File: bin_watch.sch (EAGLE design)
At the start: 88 parts, among them IC1 MEGA48/88/168-AU, J1 USB3100-XX-X_REVB, Q1 32.768kHz, T1 2N7002BKV, T2 2N7002BKV, T3 2N7002BKV, T4 2N7002BKV, T5 PMDT670UPE, T6 PMDT670UPE, T7 PMDT670UPE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

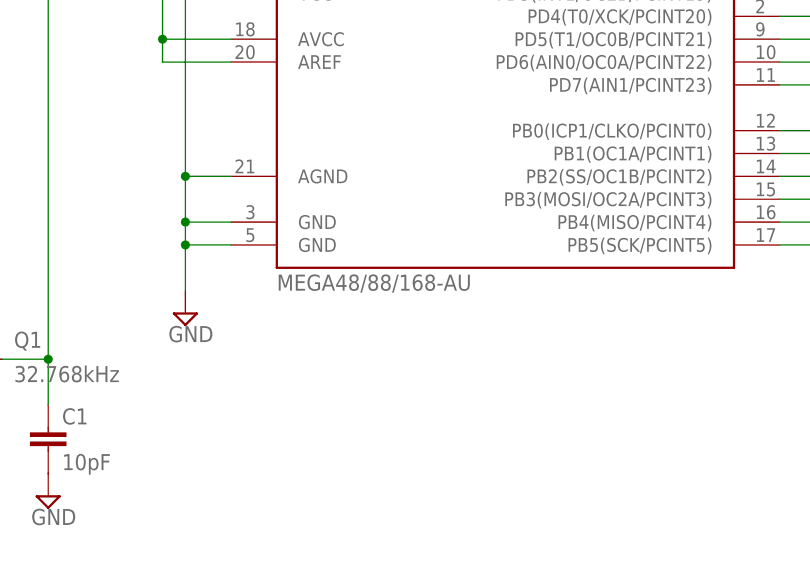
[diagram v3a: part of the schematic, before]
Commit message: QFN
ATmega328 now a QFN-32
TODO: place components, route
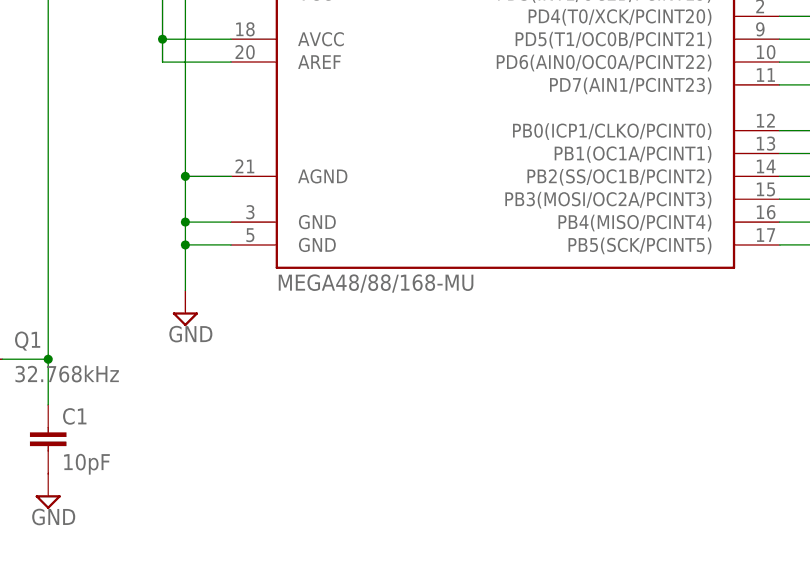
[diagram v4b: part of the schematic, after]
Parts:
- IC1: value MEGA48/88/168-AU -> MEGA48/88/168-MU; device avr-5:MEGA48/88/168-AU -> avr-5:MEGA48/88/168-MU
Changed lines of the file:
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@@
 </variantdefs>
 <classes>
-<class number="0" name="default" width="0.16" drill="0">
+<class number="0" name="default" width="0.16" drill="0.3">
 <clearance class="0" value="0.16"/>
 </class>
-<class number="1" name="supply" width="0.2" drill="0">
+<class number="1" name="supply" width="0.2" drill="0.35">
 <clearance class="1" value="0.2"/>
 </class>
-<class number="2" name="clock" width="0.16" drill="0">
+<class number="2" name="clock" width="0.16" drill="0.3">
 <clearance class="2" value="0.2"/>
 </class>
-<class number="3" name="pwr" width="0.2" drill="0">
+<class number="3" name="pwr" width="0.2" drill="0.35">
 <clearance class="3" value="0.2"/>
+</class>
+<class number="4" name="signal" width="0.127" drill="0.254">
+<clearance class="4" value="0.127"/>
 </class>
 </classes>
@@
 <part name="SUPPLY2" library="supply2" library_urn="urn:adsk.eagle:library:372" deviceset="GND" device=""/>
 <part name="JP1" library="avr-5" deviceset="AVR-ISP-6" device=""/>
-<part name="IC1" library="avr-5" deviceset="MEGA48/88/168" device="-AU"/>
+<part name="IC1" library="avr-5" deviceset="MEGA48/88/168" device="-MU" value="MEGA48/88/168-MU"/>
 <part name="SUPPLY3" library="supply2" library_urn="urn:adsk.eagle:library:372" deviceset="GND" device=""/>
 <part name="D5" library="standardparts" deviceset="LED" device=".0603" value="RG"/>
@@
 </segment>
 </net>
-<net name="GND" class="1">
+<net name="GND" class="4">
 <segment>
 <pinref part="C1" gate="G$1" pin="2"/>
@@
 </segment>
 </net>
-<net name="RST" class="0">
+<net name="RST" class="4">
 <segment>
 <pinref part="JP1" gate="G$1" pin="5"/>
@@
 </segment>
 </net>
-<net name="SCK" class="0">
+<net name="SCK" class="4">
 <segment>
 <pinref part="JP1" gate="G$1" pin="3"/>
@@
 </segment>
 </net>
-<net name="MOSI" class="0">
+<net name="MOSI" class="4">
 <segment>
 <pinref part="JP1" gate="G$1" pin="4"/>
@@
 </segment>
 </net>
-<net name="MISO" class="0">
+<net name="MISO" class="4">
 <segment>
 <pinref part="JP1" gate="G$1" pin="1"/>
@@
 </segment>
 </net>
-<net name="PB0" class="0">
+<net name="PB0" class="4">
 <segment>
 <pinref part="IC1" gate="1" pin="PB0(ICP1/CLKO/PCINT0)"/>
@@
 </segment>
 </net>
-<net name="PB1" class="0">
+<net name="PB1" class="4">
 <segment>
 <pinref part="IC1" gate="1" pin="PB1(OC1A/PCINT1)"/>
@@
 </segment>
 </net>
-<net name="PB2" class="0">
+<net name="PB2" class="4">
 <segment>
 <pinref part="IC1" gate="1" pin="PB2(SS/OC1B/PCINT2)"/>
@@
 </segment>
 </net>
-<net name="PC0" class="0">
+<net name="PC0" class="4">
 <segment>
 <pinref part="IC1" gate="1" pin="PC0(ADC0/PCINT8)"/>
@@
 </segment>
 </net>
-<net name="PC1" class="0">
+<net name="PC1" class="4">
 <segment>
 <pinref part="IC1" gate="1" pin="PC1(ADC1/PCINT9)"/>
@@
 </segment>
 </net>
-<net name="PC2" class="0">
+<net name="PC2" class="4">
 <segment>
 <pinref part="IC1" gate="1" pin="PC2(ADC2/PCINT10)"/>
@@
 </segment>
 </net>
-<net name="PC3" class="0">
+<net name="PC3" class="4">
 <segment>
 <pinref part="IC1" gate="1" pin="PC3(ADC3/PCINT11)"/>
@@
 </segment>
 </net>
-<net name="PC4" class="0">
+<net name="PC4" class="4">
 <segment>
 <pinref part="IC1" gate="1" pin="PC4(ADC4/SDA/PCINT12)"/>
@@
 </segment>
 </net>
-<net name="PC5" class="0">
+<net name="PC5" class="4">
 <segment>
 <pinref part="IC1" gate="1" pin="PC5(ADC5/SCL/PCINT13)"/>
@@
 </segment>
 </net>
-<net name="PD0" class="0">
+<net name="PD0" class="4">
 <segment>
 <pinref part="IC1" gate="1" pin="PD0(RXD/PCINT16)"/>
@@
 </segment>
 </net>
-<net name="PD1" class="0">
+<net name="PD1" class="4">
 <segment>
 <pinref part="IC1" gate="1" pin="PD1(TXD/PCINT17)"/>
@@
 </segment>
 </net>
-<net name="PD2" class="0">
+<net name="PD2" class="4">
 <segment>
 <pinref part="IC1" gate="1" pin="PD2(INT0/PCINT18)"/>
@@
 </segment>
 </net>
-<net name="PD3" class="0">
+<net name="PD3" class="4">
 <segment>
 <pinref part="IC1" gate="1" pin="PD3(INT1/OC2B/PCINT19)"/>
@@
 </segment>
 </net>
-<net name="PD4" class="0">
+<net name="PD4" class="4">
 <segment>
 <pinref part="IC1" gate="1" pin="PD4(T0/XCK/PCINT20)"/>
@@
 </segment>
 </net>
-<net name="PD5" class="0">
+<net name="PD5" class="4">
 <segment>
 <pinref part="IC1" gate="1" pin="PD5(T1/OC0B/PCINT21)"/>
@@
 </segment>
 </net>
-<net name="PD6" class="0">
+<net name="PD6" class="4">
 <segment>
 <pinref part="IC1" gate="1" pin="PD6(AIN0/OC0A/PCINT22)"/>
@@
 </segment>
 </net>
-<net name="PD7" class="0">
+<net name="PD7" class="4">
 <segment>
 <pinref part="IC1" gate="1" pin="PD7(AIN1/PCINT23)"/>
@@
 </segment>
 </net>
-<net name="PROG" class="0">
+<net name="PROG" class="4">
 <segment>
 <pinref part="U1" gate="A" pin="PROG"/>

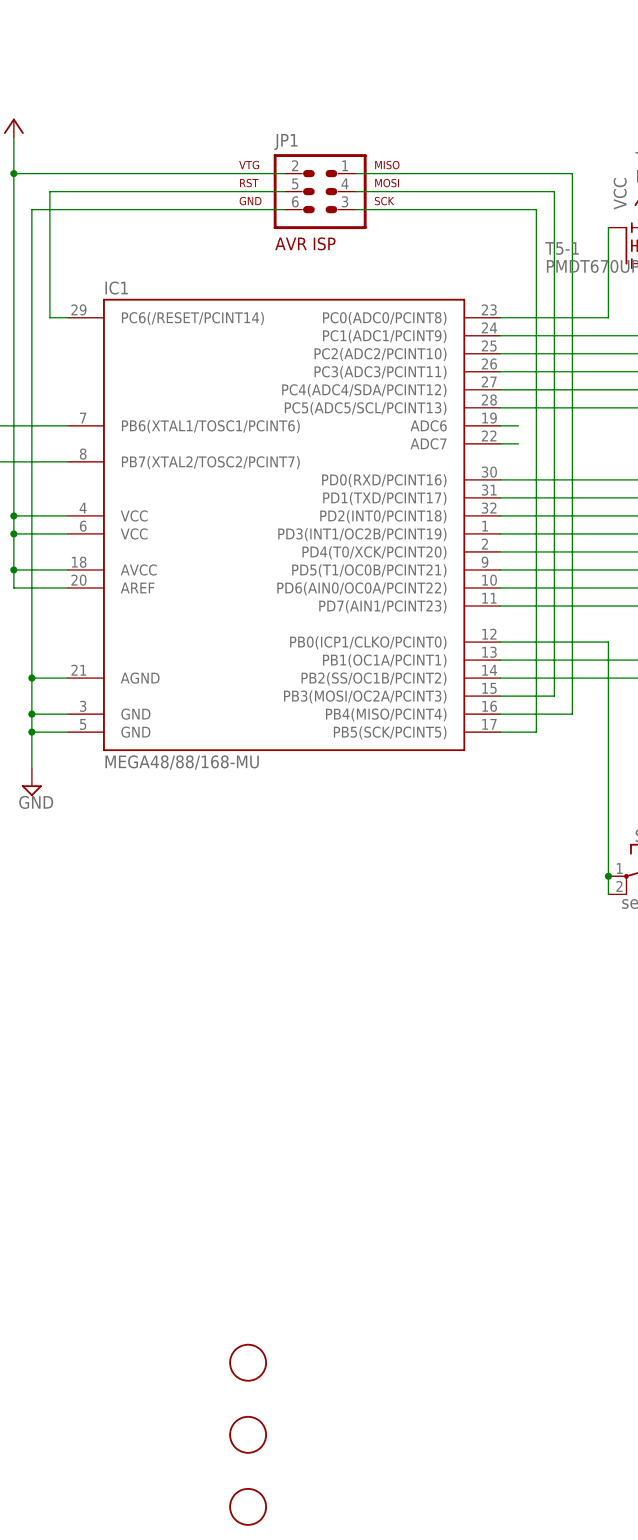
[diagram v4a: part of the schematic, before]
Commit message: Replaced AVR ISP with smaller pads
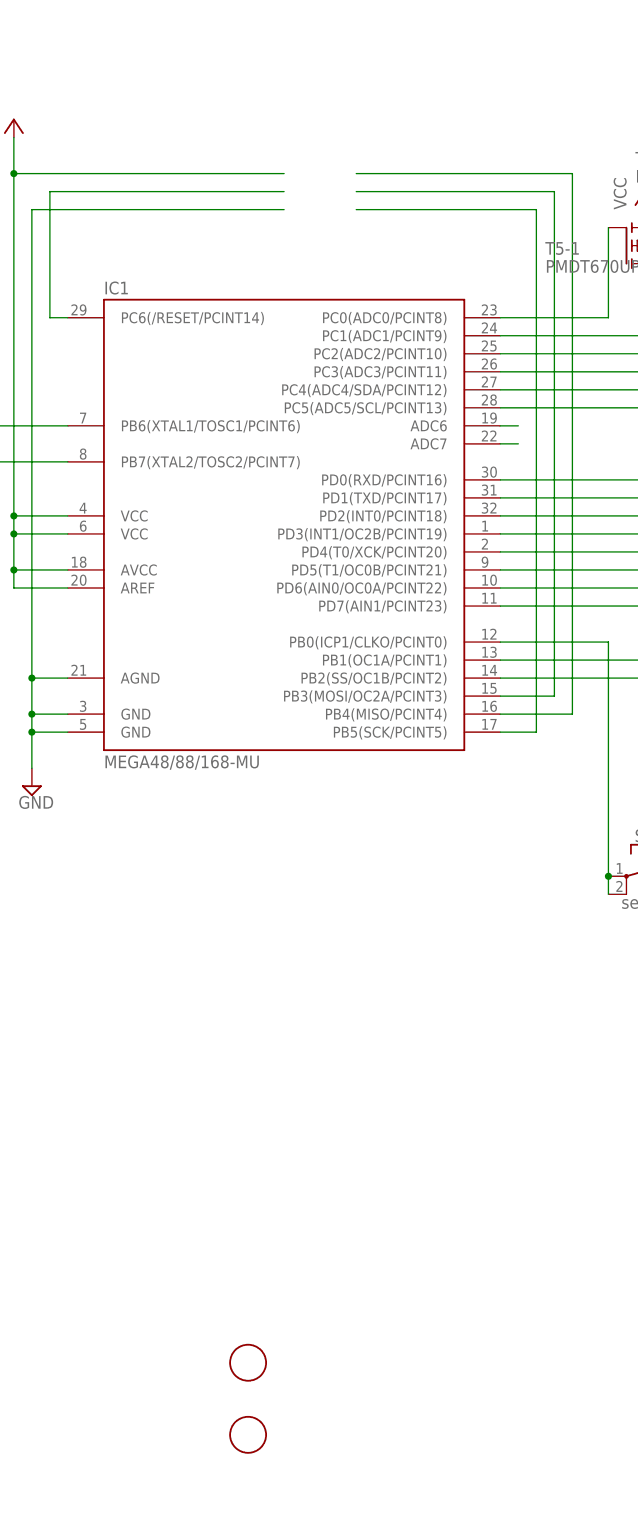
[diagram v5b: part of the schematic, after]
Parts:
- removed JP1: AVR-ISP-6, avr-5:AVR-ISP-6
- removed U$3: FIDUCIAL, adafruit:FIDUCIAL
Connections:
- net GND: no longer JP1.6
- net MISO: no longer JP1.1
- net MOSI: no longer JP1.4
- net RST: no longer JP1.5
- net SCK: no longer JP1.3
- net VCC: no longer JP1.2
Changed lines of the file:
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@@
 <clearance class="3" value="0.2"/>
 </class>
-<class number="4" name="signal" width="0.127" drill="0.254">
-<clearance class="4" value="0.127"/>
+<class number="4" name="signal" width="0.13" drill="0.254">
+<clearance class="4" value="0.13"/>
 </class>
 </classes>
@@
 <part name="C1" library="rcl" library_urn="urn:adsk.eagle:library:334" deviceset="C-EU" device="C0603" package3d_urn="urn:adsk.eagle:package:23616/2" value="10pF"/>
 <part name="SUPPLY2" library="supply2" library_urn="urn:adsk.eagle:library:372" deviceset="GND" device=""/>
-<part name="JP1" library="avr-5" deviceset="AVR-ISP-6" device=""/>
 <part name="IC1" library="avr-5" deviceset="MEGA48/88/168" device="-MU" value="MEGA48/88/168-MU"/>
 <part name="SUPPLY3" library="supply2" library_urn="urn:adsk.eagle:library:372" deviceset="GND" device=""/>
@@
 <part name="U$1" library="adafruit" library_urn="urn:adsk.eagle:library:420" deviceset="FIDUCIAL" device=""/>
 <part name="U$2" library="adafruit" library_urn="urn:adsk.eagle:library:420" deviceset="FIDUCIAL" device=""/>
-<part name="U$3" library="adafruit" library_urn="urn:adsk.eagle:library:420" deviceset="FIDUCIAL" device=""/>
 <part name="U2" library="Texas Instruments_By_element14_Batch_1" deviceset="TPS61240DRVT" device=""/>
 <part name="P+8" library="supply1" library_urn="urn:adsk.eagle:library:371" deviceset="VCC" device=""/>
@@
 <instance part="C1" gate="G$1" x="43.18" y="15.24"/>
 <instance part="SUPPLY2" gate="GND" x="43.18" y="7.62"/>
-<instance part="JP1" gate="G$1" x="99.06" y="111.76"/>
 <instance part="IC1" gate="1" x="93.98" y="66.04"/>
 <instance part="SUPPLY3" gate="GND" x="58.42" y="27.94"/>
@@
 <instance part="U$1" gate="G$1" x="88.9" y="-53.34"/>
 <instance part="U$2" gate="G$1" x="88.9" y="-63.5"/>
-<instance part="U$3" gate="G$1" x="88.9" y="-73.66"/>
 <instance part="U2" gate="A" x="254" y="248.92"/>
 <instance part="P+8" gate="VCC" x="281.94" y="284.48"/>
@@
 </segment>
 </net>
-<net name="GND" class="4">
+<net name="GND" class="1">
 <segment>
 <pinref part="C1" gate="G$1" pin="2"/>
@@
 </segment>
 <segment>
-<pinref part="JP1" gate="G$1" pin="6"/>
 <wire x1="93.98" y1="109.22" x2="58.42" y2="109.22" width="0.1524" layer="91"/>
 <wire x1="58.42" y1="109.22" x2="58.42" y2="43.18" width="0.1524" layer="91"/>
@@
 <net name="RST" class="4">
 <segment>
-<pinref part="JP1" gate="G$1" pin="5"/>
 <wire x1="93.98" y1="111.76" x2="60.96" y2="111.76" width="0.1524" layer="91"/>
 <wire x1="60.96" y1="111.76" x2="60.96" y2="93.98" width="0.1524" layer="91"/>
@@
 <net name="SCK" class="4">
 <segment>
-<pinref part="JP1" gate="G$1" pin="3"/>
 <wire x1="104.14" y1="109.22" x2="129.54" y2="109.22" width="0.1524" layer="91"/>
 <wire x1="129.54" y1="109.22" x2="129.54" y2="35.56" width="0.1524" layer="91"/>
@@
 <net name="MOSI" class="4">
 <segment>
-<pinref part="JP1" gate="G$1" pin="4"/>
 <wire x1="104.14" y1="111.76" x2="132.08" y2="111.76" width="0.1524" layer="91"/>
 <wire x1="132.08" y1="111.76" x2="132.08" y2="40.64" width="0.1524" layer="91"/>
@@
 <net name="MISO" class="4">
 <segment>
-<pinref part="JP1" gate="G$1" pin="1"/>
 <wire x1="104.14" y1="114.3" x2="134.62" y2="114.3" width="0.1524" layer="91"/>
 <wire x1="134.62" y1="114.3" x2="134.62" y2="38.1" width="0.1524" layer="91"/>
@@
 <net name="VCC" class="1">
 <segment>
-<pinref part="JP1" gate="G$1" pin="2"/>
 <wire x1="93.98" y1="114.3" x2="55.88" y2="114.3" width="0.1524" layer="91"/>
 <wire x1="55.88" y1="114.3" x2="55.88" y2="66.04" width="0.1524" layer="91"/>

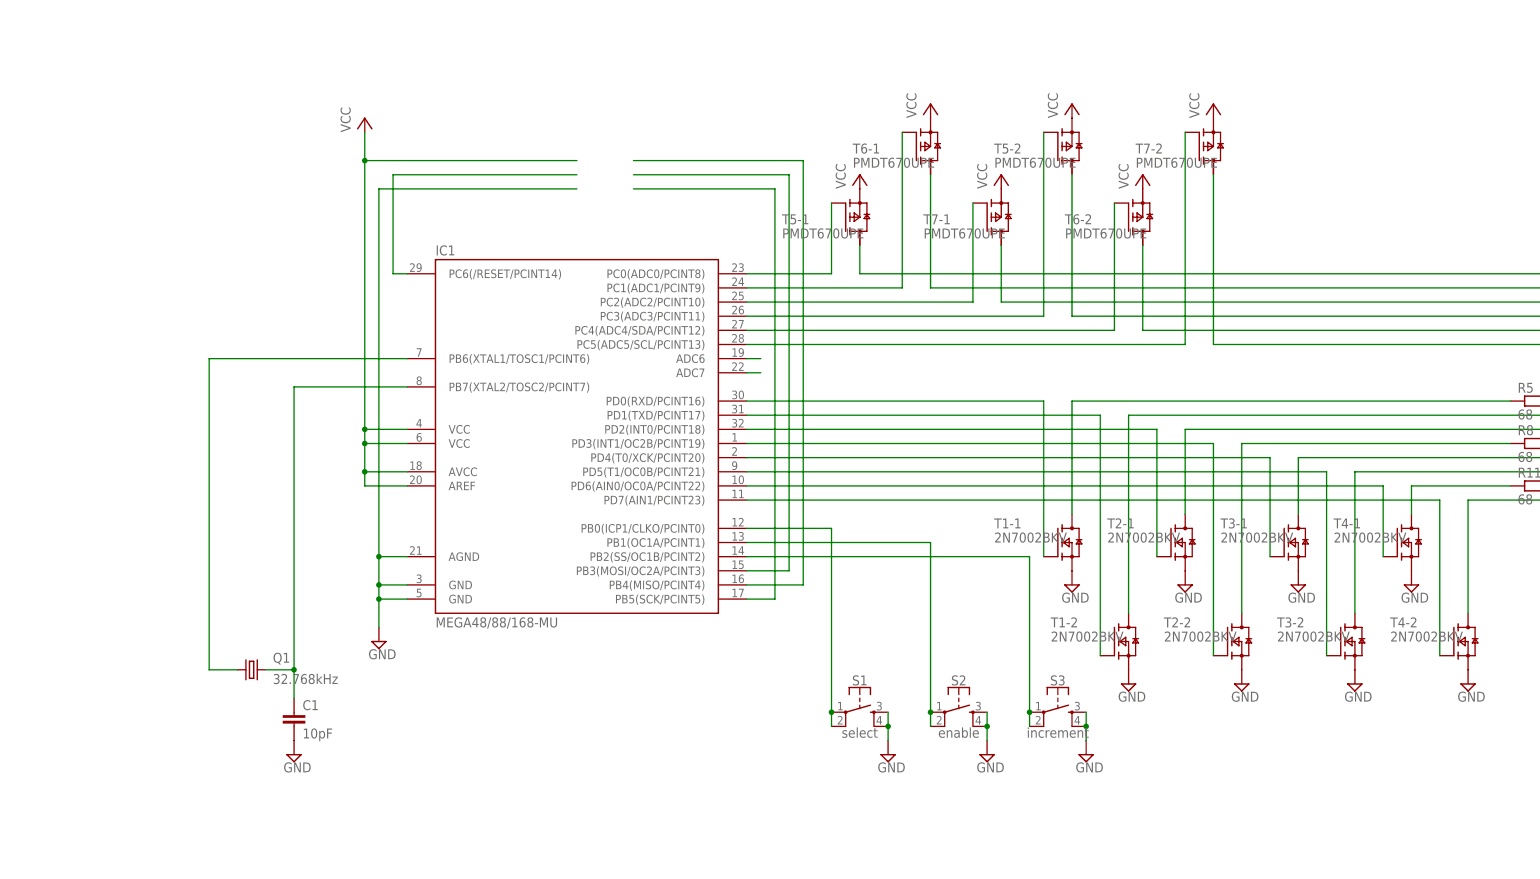
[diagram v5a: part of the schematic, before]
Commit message: IOs rewired
Changed the IO wiring to reduce the number of vias.
TODO: Power supply routing
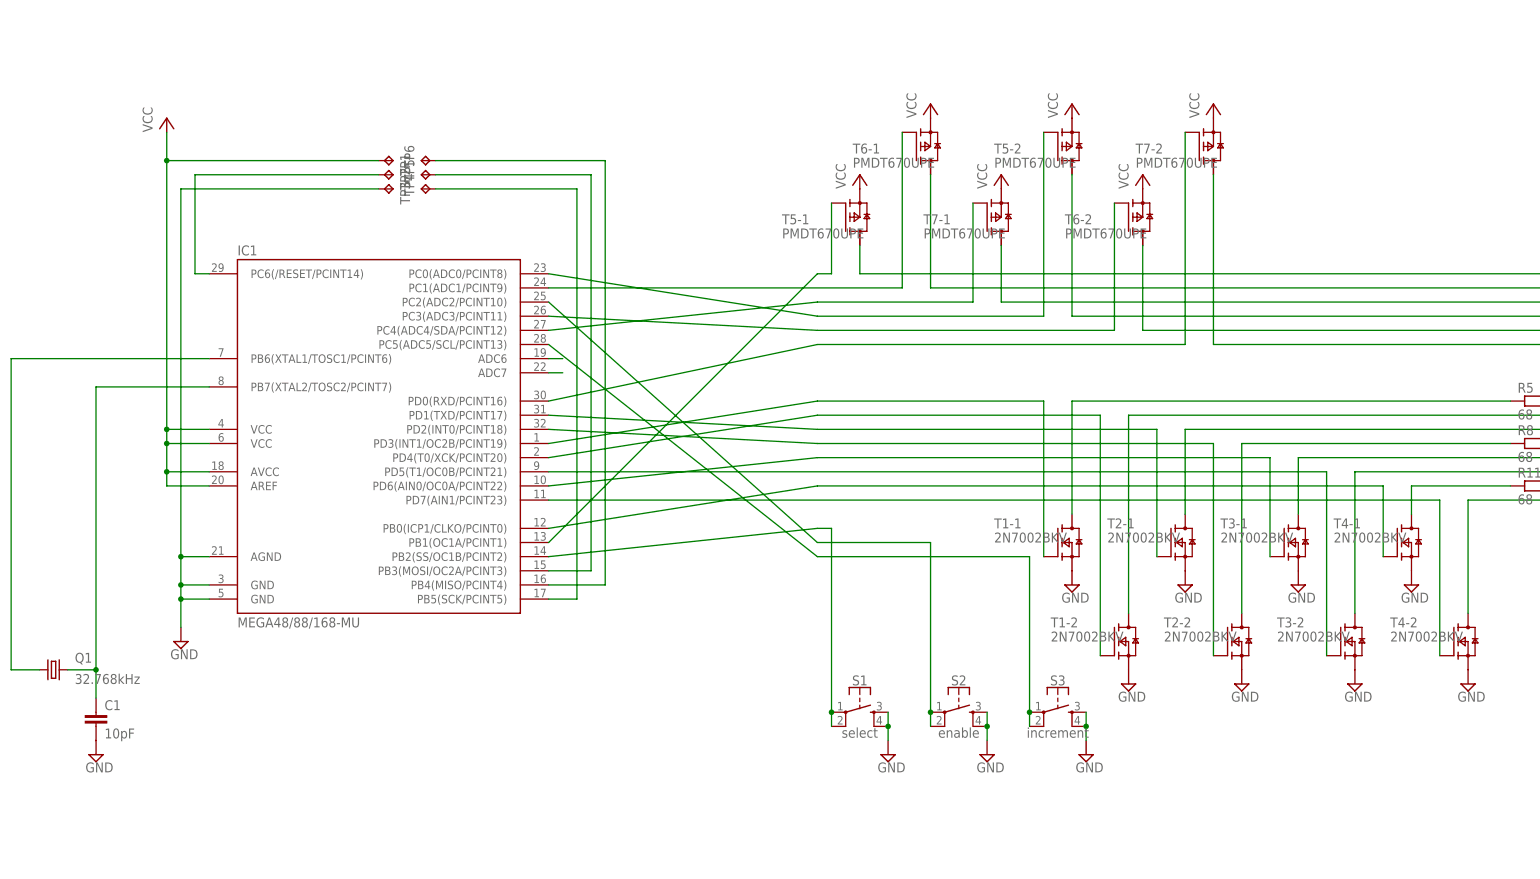
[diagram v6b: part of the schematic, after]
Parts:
- added TP1, TP2, TP3, TP4, TP5, TP6: TPTP07SQ, testpad:TPTP07SQ
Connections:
- net GND: now also TP3.TP
- net MISO: now also TP6.TP
- net MOSI: now also TP5.TP
- net PB0: now also IC1.PB2(SS/OC1B/PCINT2); no longer IC1.PB0(ICP1/CLKO/PCINT0)
- net PB1: now also IC1.PC2(ADC2/PCINT10); no longer IC1.PB1(OC1A/PCINT1)
- net PB2: now also IC1.PC5(ADC5/SCL/PCINT13); no longer IC1.PB2(SS/OC1B/PCINT2)
- net PC0: now also IC1.PB1(OC1A/PCINT1); no longer IC1.PC0(ADC0/PCINT8)
- net PC2: now also IC1.PC4(ADC4/SDA/PCINT12); no longer IC1.PC2(ADC2/PCINT10)
- net PC3: now also IC1.PC0(ADC0/PCINT8); no longer IC1.PC3(ADC3/PCINT11)
- net PC4: now also IC1.PC3(ADC3/PCINT11); no longer IC1.PC4(ADC4/SDA/PCINT12)
- net PC5: now also IC1.PD0(RXD/PCINT16); no longer IC1.PC5(ADC5/SCL/PCINT13)
- net PD0: now also IC1.PD3(INT1/OC2B/PCINT19); no longer IC1.PD0(RXD/PCINT16)
- net PD1: now also IC1.PD4(T0/XCK/PCINT20); no longer IC1.PD1(TXD/PCINT17)
- net PD2: now also IC1.PD1(TXD/PCINT17); no longer IC1.PD2(INT0/PCINT18)
- net PD3: now also IC1.PD2(INT0/PCINT18); no longer IC1.PD3(INT1/OC2B/PCINT19)
- net PD4: now also IC1.PD6(AIN0/OC0A/PCINT22); no longer IC1.PD4(T0/XCK/PCINT20)
- net PD6: now also IC1.PB0(ICP1/CLKO/PCINT0); no longer IC1.PD6(AIN0/OC0A/PCINT22)
- net RST: now also TP2.TP
- net SCK: now also TP4.TP
- net VCC: now also TP1.TP
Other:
- moved on the sheet: C1, IC1, Q1
